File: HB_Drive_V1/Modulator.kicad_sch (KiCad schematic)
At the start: 1 part, among them J7 Conn_02x04_Counter_Clockwise

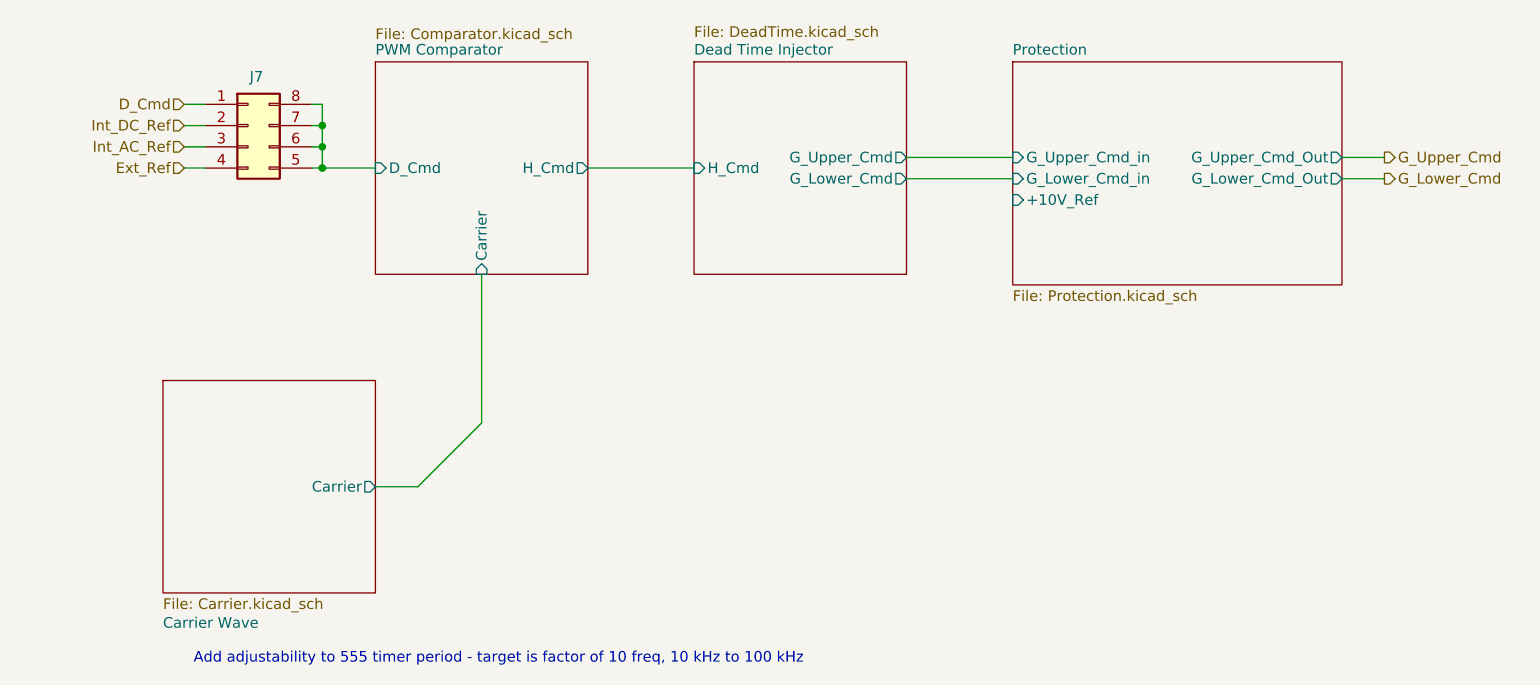
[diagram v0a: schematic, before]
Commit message: finishes hirearchical labels, add 10v +- ref generation and updates the DC offset circuits
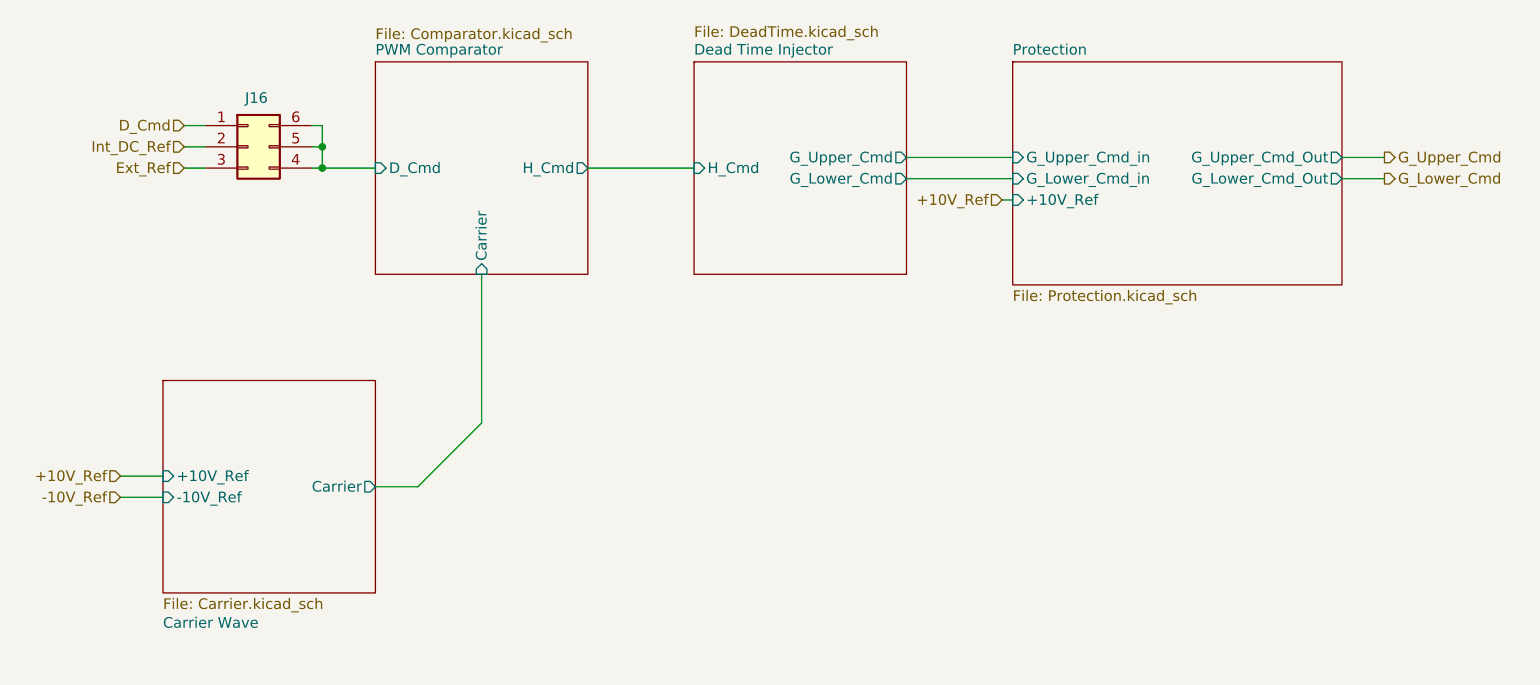
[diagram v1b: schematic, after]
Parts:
- removed J7: Conn_02x04_Counter_Clockwise, Connector_PinSocket_1.27mm:PinSocket_2x04_P1.27mm_Vertical, symbol Connector_Generic:Conn_02x04_Counter_Clockwise
- added J16: Conn_02x03_Counter_Clockwise, Connector_PinSocket_1.27mm:PinSocket_2x03_P1.27mm_Vertical, symbol Connector_Generic:Conn_02x03_Counter_Clockwise
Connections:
- net D_Cmd: now also J16.1 (Pin_1)
- net Ext_Ref: now also J16.3 (Pin_3)
- net Int_DC_Ref: now also J16.2 (Pin_2)
- net PWM Comparator/D_Cmd: now also J16.4 (Pin_4), J16.5 (Pin_5), J16.6 (Pin_6)
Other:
- sheet Carrier Wave ports: added +10V_Ref, -10V_Ref; removed none
- note removed: "Add adjustability to 555 timer period - target is factor of 10 freq, 10 kHz to 100 kHz"

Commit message: updates board to highest working copy
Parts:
- removed J16: Conn_02x03_Counter_Clockwise, Connector_PinSocket_1.27mm:PinSocket_2x03_P1.27mm_Vertical, symbol Connector_Generic:Conn_02x03_Counter_Clockwise
- added J801: Conn_02x03_Odd_Even, Connector_PinHeader_2.54mm:PinHeader_2x03_P2.54mm_Vertical, symbol Connector_Generic:Conn_02x03_Odd_Even
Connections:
- net D_Cmd: now also J801.1 (Pin_1)
- new net Ext_Cmd: J801.5 (Pin_5)
- new net Int_Cmd: J801.3 (Pin_3)
- new net Modulator and Dead Time Injector/D_Cmd: J801.2 (Pin_2), J801.4 (Pin_4), J801.6 (Pin_6)
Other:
- removed sheet Dead Time Injector
- removed sheet PWM Comparator
- added sheet Modulator and Dead Time Injector (ModAndDead.kicad_sch)
- sheet Protection ports: added I_Fdbk_Raw; removed none

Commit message: removes Aux file trouble
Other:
- sheet Protection ports: added I_Fdbk; removed I_Fdbk_Raw
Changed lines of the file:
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@@
 		)
 	)
-	(hierarchical_label "I_Fdbk_Raw"
+	(hierarchical_label "I_Fdbk"
 		(shape input)
 		(at 146.05 83.82 180)
@@
 			)
 		)
-		(pin "I_Fdbk_Raw" input
+		(pin "I_Fdbk" input
 			(at 151.13 83.82 180)
 			(effects

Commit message: updates board to REV 1 Ordered version
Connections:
- net D_Cmd: now also J801.5 (Pin_5); no longer J801.1 (Pin_1)
- net Ext_Cmd: now also J801.3 (Pin_3); no longer J801.5 (Pin_5)
- net Int_Cmd: now also J801.1 (Pin_1); no longer J801.3 (Pin_3)
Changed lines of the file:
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@@
-		)
-	)
-	(hierarchical_label "D_Cmd"
-		(shape input)
-		(at 78.74 71.12 180)
-		(effects
-			(font
-				(size 1.27 1.27)
-			)
-			(justify right)
-		)
-	)
-	(hierarchical_label "Int_Cmd"
-		(shape input)
-		(at 78.74 73.66 180)
-		(effects
-			(font
-				(size 1.27 1.27)
-			)
-			(justify right)
 		)
 	)
@@
 		)
 	)
+	(hierarchical_label "Int_Cmd"
+		(shape input)
+		(at 78.74 71.12 180)
+		(effects
+			(font
+				(size 1.27 1.27)
+			)
+			(justify right)
+		)
+	)
 	(hierarchical_label "+10V_Ref"
 		(shape input)
@@
 		)
 	)
-	(hierarchical_label "Ext_Cmd"
+	(hierarchical_label "-10V_Ref"
 		(shape input)
-		(at 78.74 76.2 180)
+		(at 71.12 115.57 180)
 		(effects
 			(font
@@
 		)
 	)
-	(hierarchical_label "-10V_Ref"
+	(hierarchical_label "Ext_Cmd"
 		(shape input)
-		(at 71.12 115.57 180)
+		(at 78.74 73.66 180)
 		(effects
 			(font
+				(size 1.27 1.27)
+			)
+			(justify right)
+		)
+	)
+	(hierarchical_label "D_Cmd"
+		(shape input)
+		(at 78.74 76.2 180)
+		(effects
+			(font

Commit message: Annotates Schematic! Fixes REV1 wiring swaps and replaces buffer
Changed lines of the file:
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@@
+	(wire
+		(pts
+			(xy 127 74.93) (xy 151.13 74.93)
+		)
+		(stroke
+			(width 0)
+			(type default)
+		)
+	)
 	(wire
 		(pts
@@
 	(wire
 		(pts
-			(xy 127 74.93) (xy 151.13 74.93)
-		)
-		(stroke
-			(width 0)
-			(type default)
-		)
-	)
-	(wire
-		(pts
 			(xy 95.25 73.66) (xy 95.25 76.2)
 		)
@@
 		)
 	)
-	(hierarchical_label "I_Fdbk"
+	(hierarchical_label "-I_Fdbk"
 		(shape input)
 		(at 146.05 83.82 180)
@@
 			)
 		)
+		(property "Sim.Device" ""
+			(at 86.36 73.66 0)
+			(hide yes)
+			(show_name no)
+			(do_not_autoplace no)
+			(effects
+				(font
+					(size 1.27 1.27)
+				)
+			)
+		)
 		(pin "4"
 		)
@@
 		)
 		(pin "G_Lower_Cmd" output
+			(at 127 77.47 0)
+			(effects
+				(font
+					(size 1.27 1.27)
+				)
+				(justify right)
+			)
+		)
+		(pin "G_Upper_Cmd" output
 			(at 127 74.93 0)
 			(effects
 				(font
-					(size 1.27 1.27)
-				)
-				(justify right)
-			)
-		)
-		(pin "G_Upper_Cmd" output
-			(at 127 77.47 0)
-			(effects
-				(font
